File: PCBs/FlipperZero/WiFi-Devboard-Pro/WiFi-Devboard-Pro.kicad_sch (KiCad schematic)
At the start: 33 parts

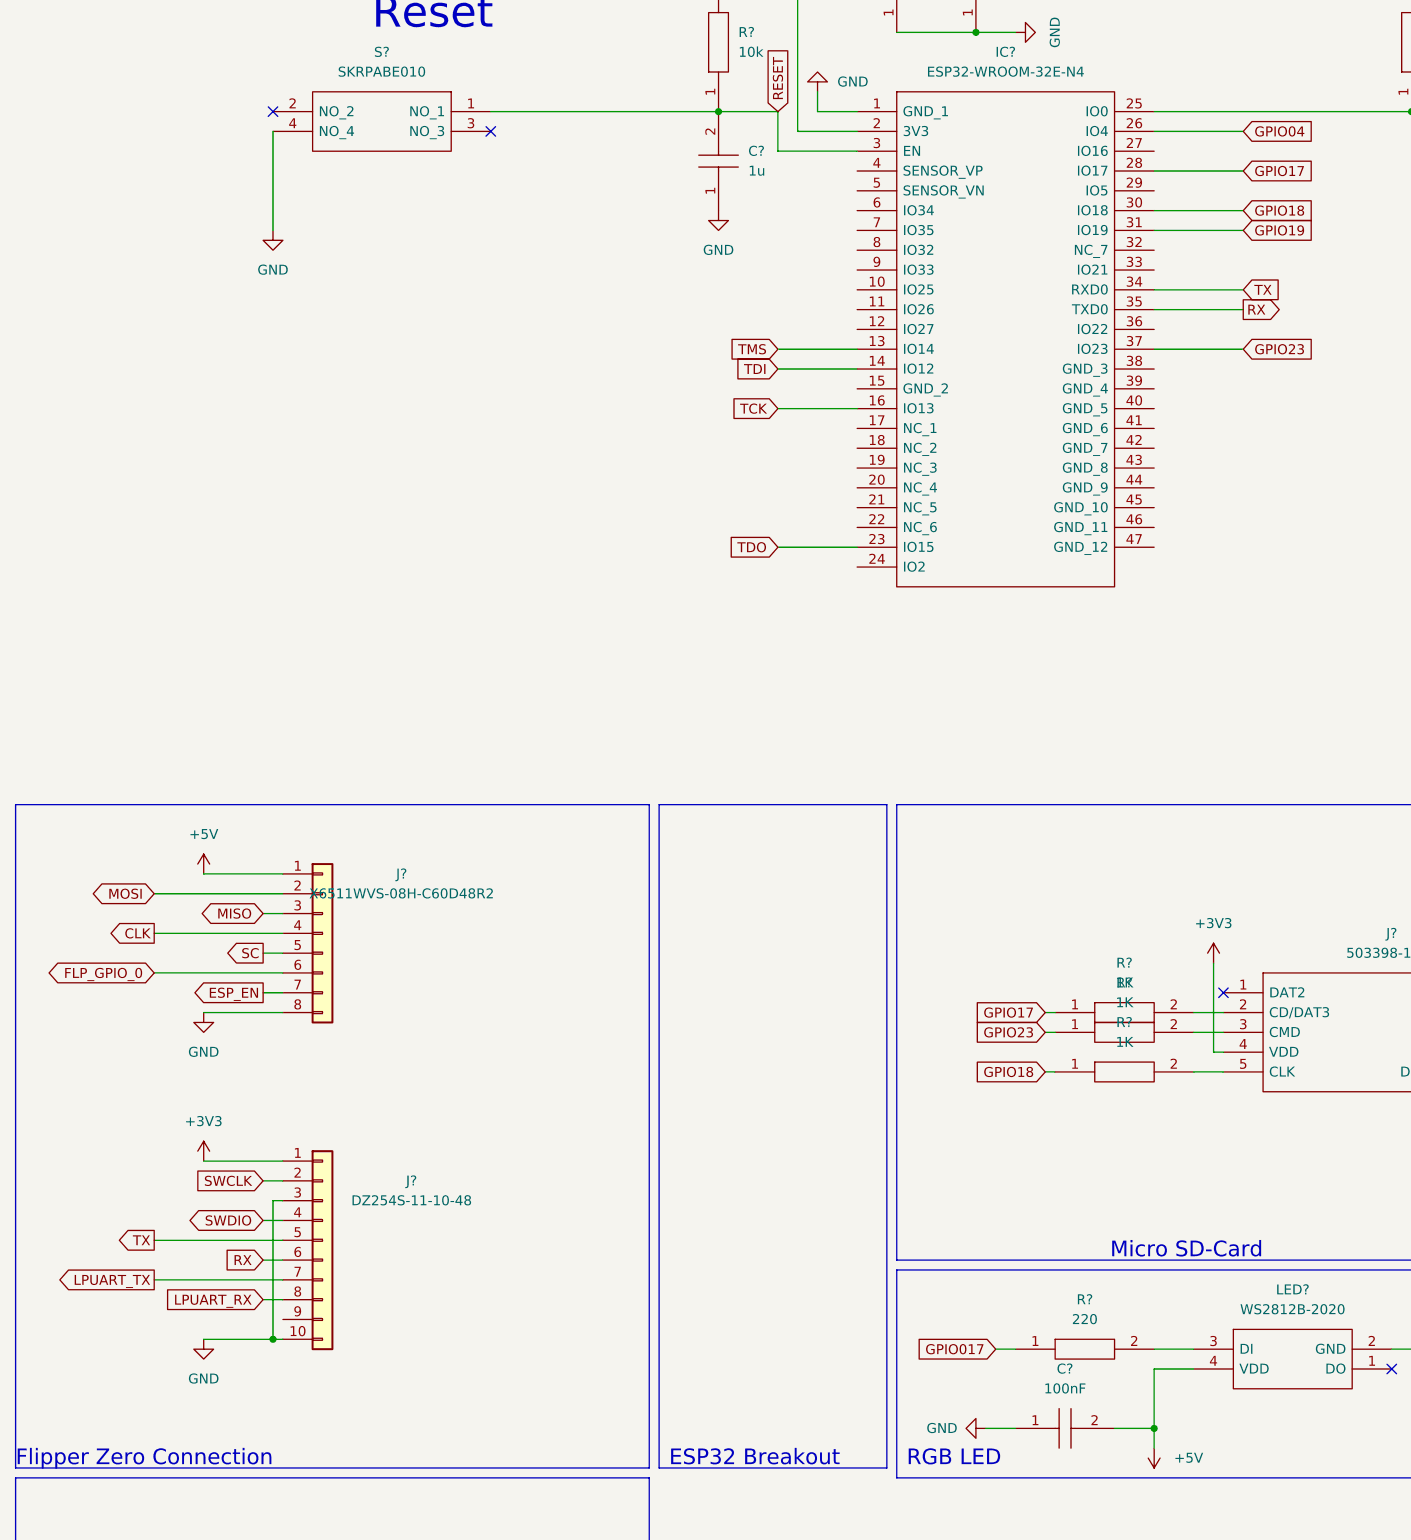
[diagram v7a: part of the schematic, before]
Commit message: Add ESP32 Breakout
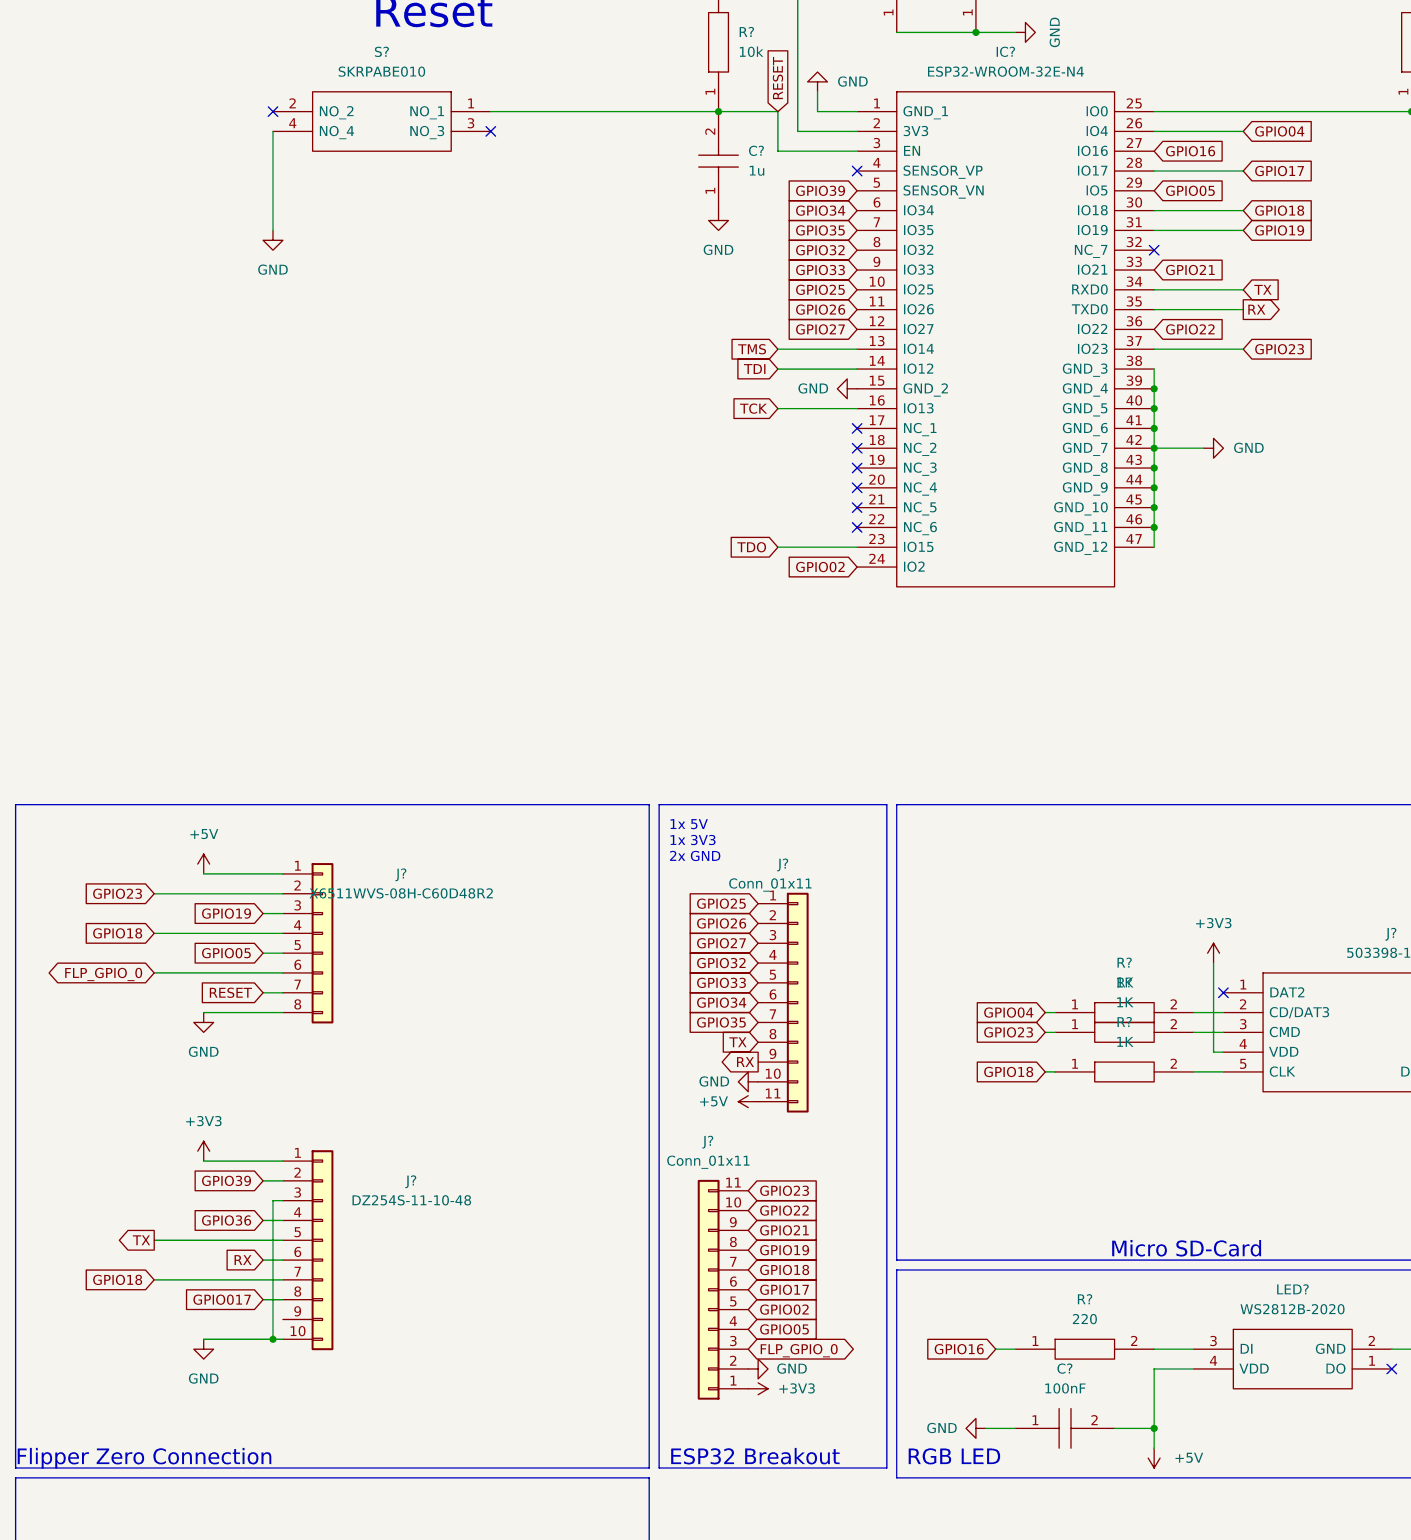
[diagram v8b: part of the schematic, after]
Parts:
- added J? (x2): Conn_01x11, symbol Connector_Generic:Conn_01x11
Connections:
- net CLK is gone; now on net GPIO18: J?.4 (Pin_4)
- net ESP_EN is gone; now on net RESET: J?.7 (Pin_7)
- net LPUART_RX is gone; now on net GPIO017: J?.8 (Pin_8)
- net LPUART_TX is gone; now on net GPIO18: J?.7 (Pin_7)
- net MISO is gone; now on net GPIO19: J?.3 (Pin_3)
- net MOSI is gone; now on net GPIO23: J?.2 (Pin_2)
- net SC is gone; now on net GPIO05: J?.5 (Pin_5)
- net SWCLK is gone; now on net GPIO39: J?.2 (Pin_2)
- net +3V3: now also J?.1 (Pin_1)
- net +5V: now also J?.11 (Pin_11)
- net FLP_GPIO_0: now also J?.3 (Pin_3)
- net GND: now also IC?.15 (GND_2), IC?.38 (GND_3), IC?.39 (GND_4), IC?.40 (GND_5), IC?.41 (GND_6), IC?.42 (GND_7), IC?.43 (GND_8), IC?.44 (GND_9), IC?.45 (GND_10), IC?.46 (GND_11), IC?.47 (GND_12), J?.10 (Pin_10), J?.2 (Pin_2)
- net GPIO017: no longer R?.1
- net GPIO04: now also R?.1
- net GPIO17: now also J?.6 (Pin_6); no longer R?.1
- net GPIO18: now also J?.7 (Pin_7)
- net GPIO19: now also J?.8 (Pin_8)
- net GPIO23: now also J?.11 (Pin_11)
- net RX: now also J?.9 (Pin_9)
- net TX: now also J?.8 (Pin_8)
- net GPIO25: now reaches IC?.10 (IO25)
- net GPIO25: now also J?.1 (Pin_1)
- net GPIO26: now reaches IC?.11 (IO26)
- net GPIO26: now also J?.2 (Pin_2)
- net GPIO27: now reaches IC?.12 (IO27)
- net GPIO27: now also J?.3 (Pin_3)
- net GPIO02: now reaches IC?.24 (IO2)
- net GPIO02: now also J?.5 (Pin_5)
- net GPIO16: now reaches IC?.27 (IO16)
- net GPIO16: now also R?.1
- net GPIO05: now reaches IC?.29 (IO5)
- net GPIO05: now also J?.4 (Pin_4)
- net GPIO21: now reaches IC?.33 (IO21)
- net GPIO21: now also J?.9 (Pin_9)
- net GPIO22: now reaches IC?.36 (IO22)
- net GPIO22: now also J?.10 (Pin_10)
- net GPIO39: now reaches IC?.5 (SENSOR_VN)
- net GPIO34: now reaches IC?.6 (IO34)
- net GPIO34: now also J?.6 (Pin_6)
- net GPIO35: now reaches IC?.7 (IO35)
- net GPIO35: now also J?.7 (Pin_7)
- net GPIO32: now reaches IC?.8 (IO32)
- net GPIO32: now also J?.4 (Pin_4)
- net GPIO33: now reaches IC?.9 (IO33)
- net GPIO33: now also J?.5 (Pin_5)
- net SWDIO renamed GPIO36
- no-connect marks 7 -> 15
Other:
- note added: "1x 5V 1x 3V3 2x GND"
